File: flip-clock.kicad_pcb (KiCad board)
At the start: 2 copper layers, 68.1 x 38.6 mm, 9 parts, among them J1 Screw_Terminal_01x02, U1 ESP-01v090, U2 AP1117-33

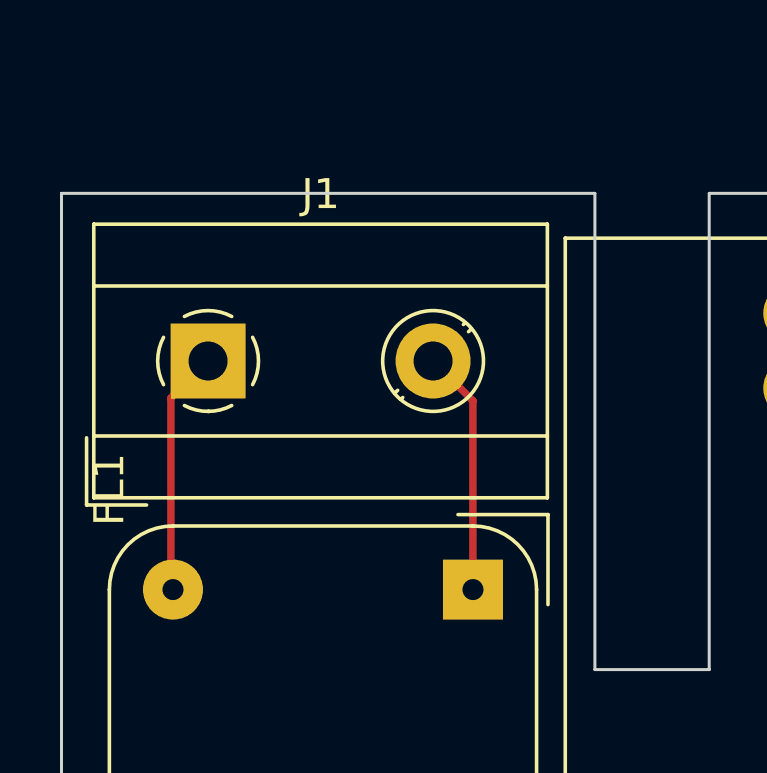
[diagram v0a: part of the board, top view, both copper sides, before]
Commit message: Added 3D models
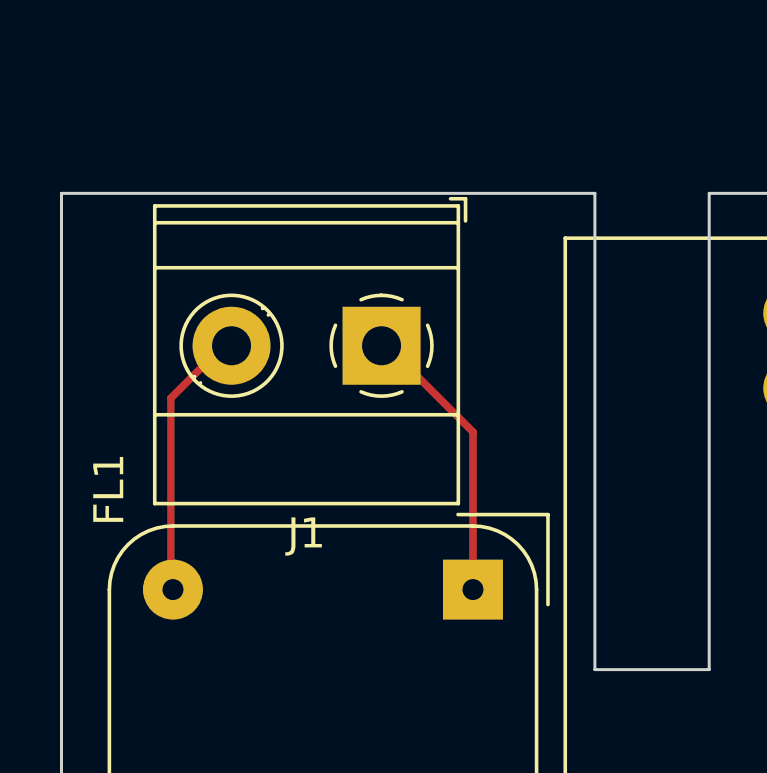
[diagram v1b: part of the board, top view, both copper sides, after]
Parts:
- J1: footprint TerminalBlock_MetzConnect:TerminalBlock_MetzConnect_Type171_RT13702HBWC_1x02_P7.50mm_Horizontal -> TerminalBlock_Phoenix:TerminalBlock_Phoenix_MKDS-1,5-2_1x02_P5.00mm_Horizontal
- moved J1 5.80 mm to (132.6, 55.9), turned to 180 degrees
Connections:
- J1 pad 1: Net-(FL1-Pad3) -> Net-(FL1-Pad1)
- J1 pad 2: Net-(FL1-Pad1) -> Net-(FL1-Pad3)
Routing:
- net Net-(FL1-Pad1): track 8.17 -> 9.49 mm
